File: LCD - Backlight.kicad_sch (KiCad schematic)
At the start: 1 part, among them IC2 TPS61165DBVR

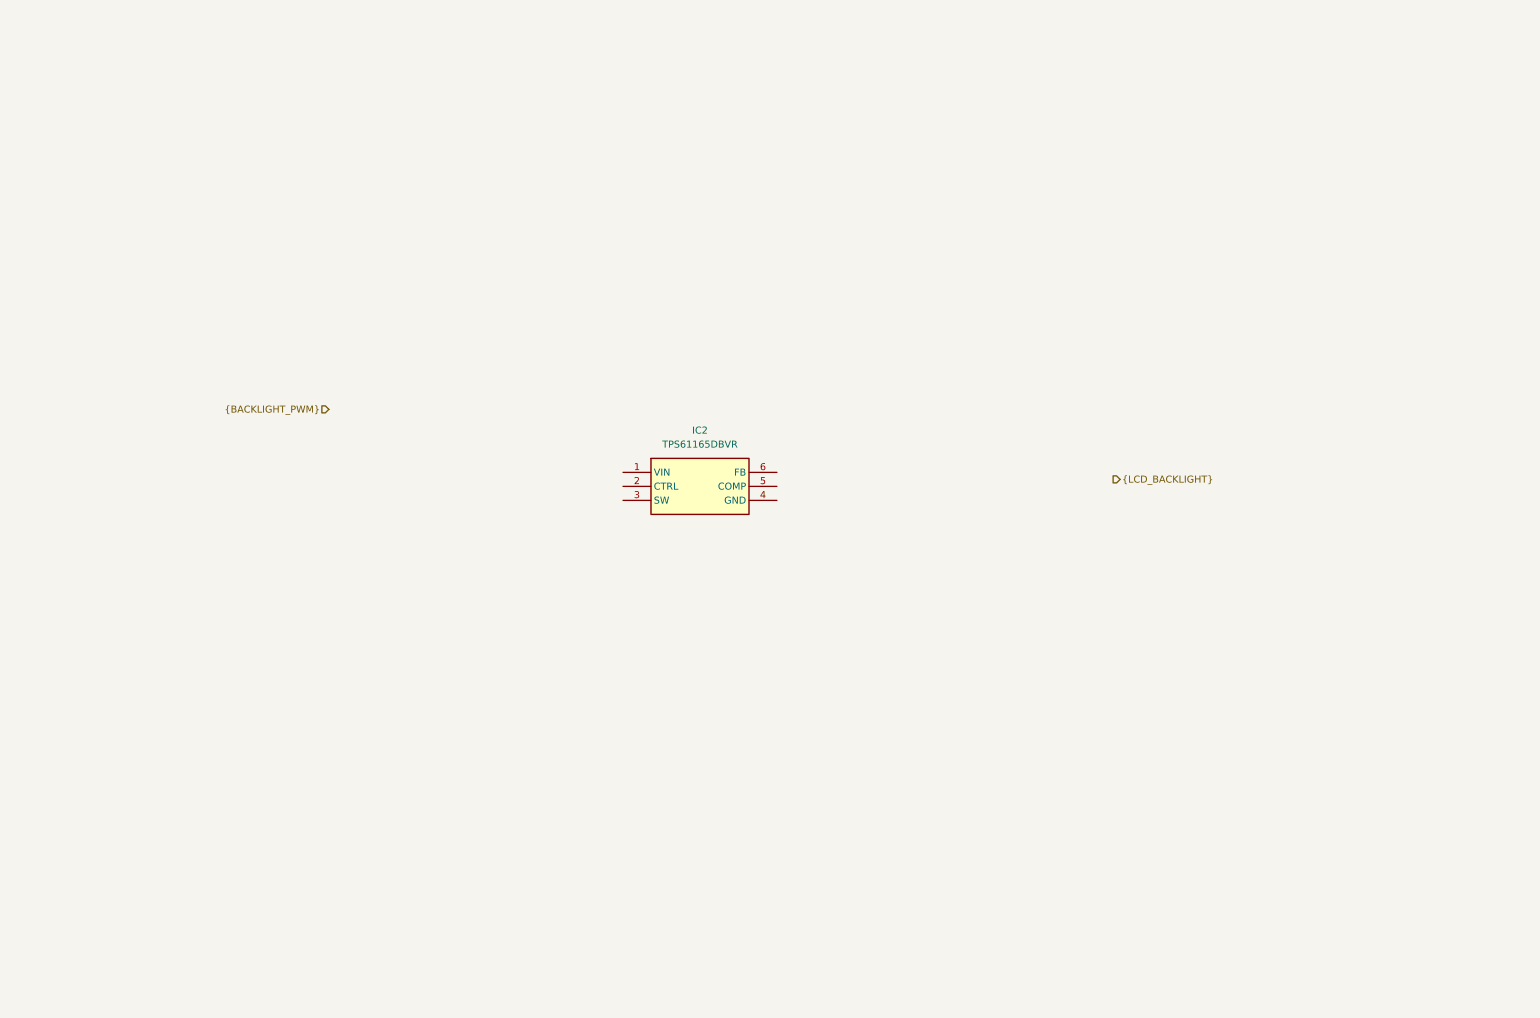
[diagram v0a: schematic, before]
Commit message: added lcd backlight schematic
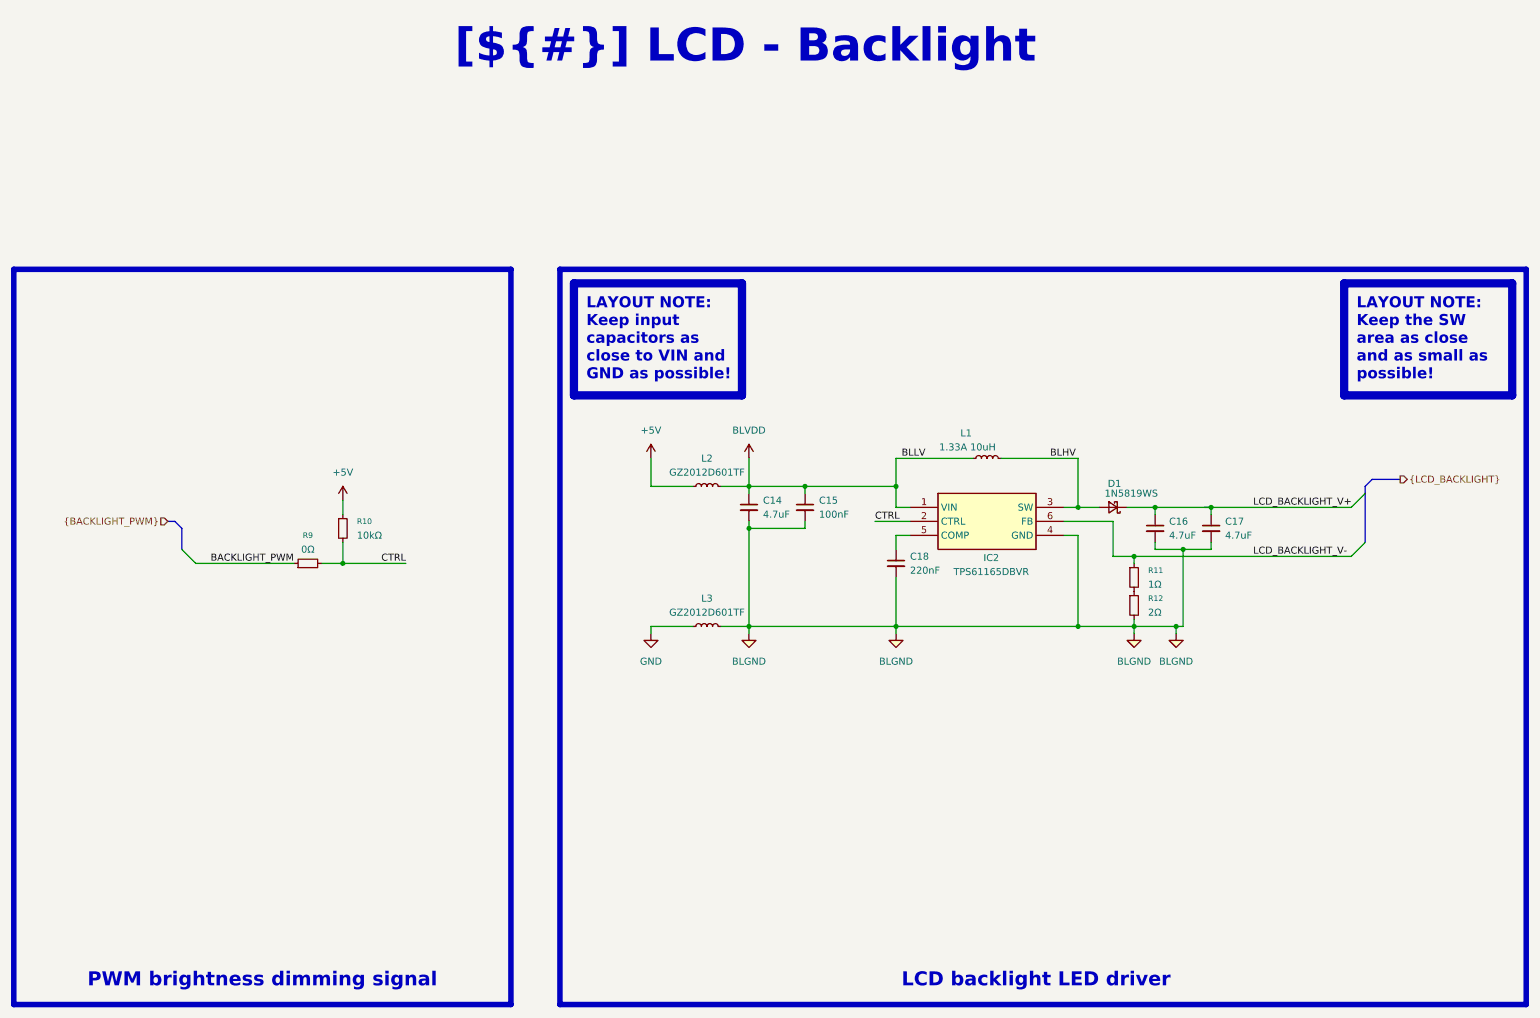
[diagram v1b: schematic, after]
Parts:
- added C14, C16, C17: 4.7uF, 0_capacitors:C_0805_2012Metric, symbol 0_capacitors:CL21A475KAQNNNE
- added C15: 100nF, 0_capacitors:C_0402_1005Metric, symbol 0_capacitors:CL05B104KO5NNNC
- added C18: 220nF, 0_capacitors:C_0402_1005Metric, symbol 0_capacitors:CL05B224KO5NNNC
- added D1: 1N5819WS, 0_diodes:D_SOD-323, symbol 0_diodes:1N5819WS
- added L1: 1.33A 10uH, 0_inductors:IND_VLS3012HBX-100M, symbol 0_inductors:VLS3012HBX-100M
- added L2, L3: GZ2012D601TF, 0_inductors:L_0805_2012Metric, symbol 0_inductors:GZ2012D601TF
- added R10: 10kΩ, 0_resistors:R_0402_1005Metric, symbol 0_resistors:0402WGF1002TCE
- added R11: 1Ω, 0_resistors:R_0603_1608Metric, symbol 0_resistors:0603WAF100KT5E
- added R12: 2Ω, 0_resistors:R_0603_1608Metric, symbol 0_resistors:0603WAF200KT5E
- added R9: 0Ω, 0_resistors:R_0402_1005Metric, symbol 0_resistors:0402WGF0000TCE
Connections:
- net BLVDD: now reaches IC2.1 (VIN)
- net BLVDD: now also C14.1, C15.1, L1.1, L2.2
- net CTRL: now reaches IC2.2 (CTRL)
- net CTRL: now also R10.2, R9.2
- net BLHV: now reaches IC2.3 (SW)
- net BLHV: now also D1.2 (A), L1.2
- net BLGND: now reaches IC2.4 (GND)
- net BLGND: now also C14.2, C15.2, C16.2, C17.2, C18.2, L3.2, R12.2
- net at IC2.5 (COMP): now also C18.1
- net LCD_BACKLIGHT_V-: now reaches IC2.6 (FB)
- net LCD_BACKLIGHT_V-: now also R11.1
- new net: R11.2, R12.1
- new net +5V: L2.1, R10.1
- new net BACKLIGHT_PWM: R9.1
- new net GND: L3.1
- new net LCD_BACKLIGHT_V+: C16.1, C17.1, D1.1 (K)
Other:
- title: (none) -> LCD - Backlight
- moved on the sheet: IC2

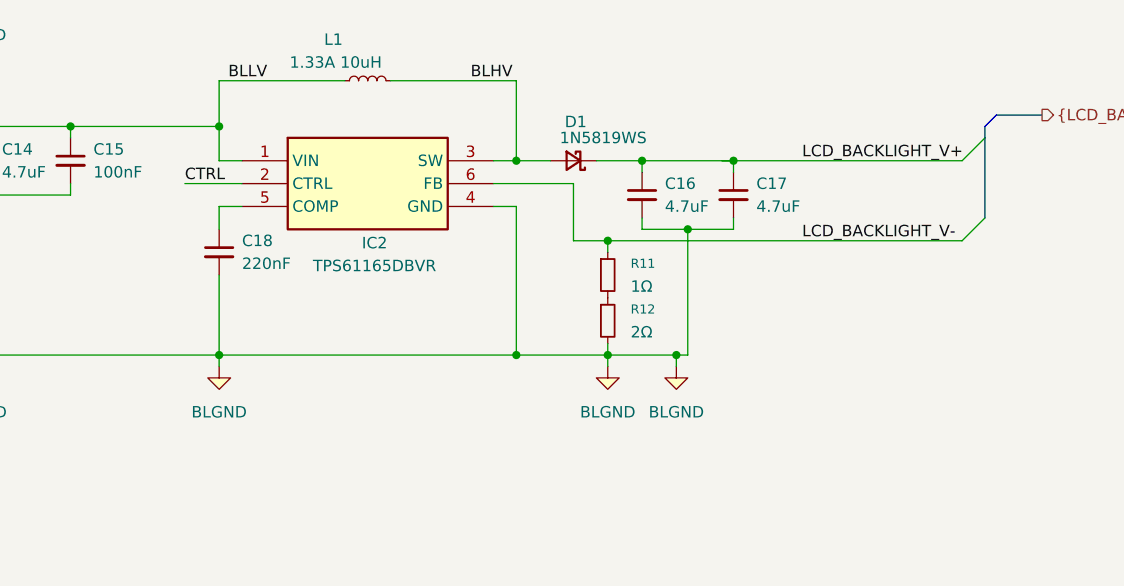
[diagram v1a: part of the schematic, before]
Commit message: added RF ransceiver
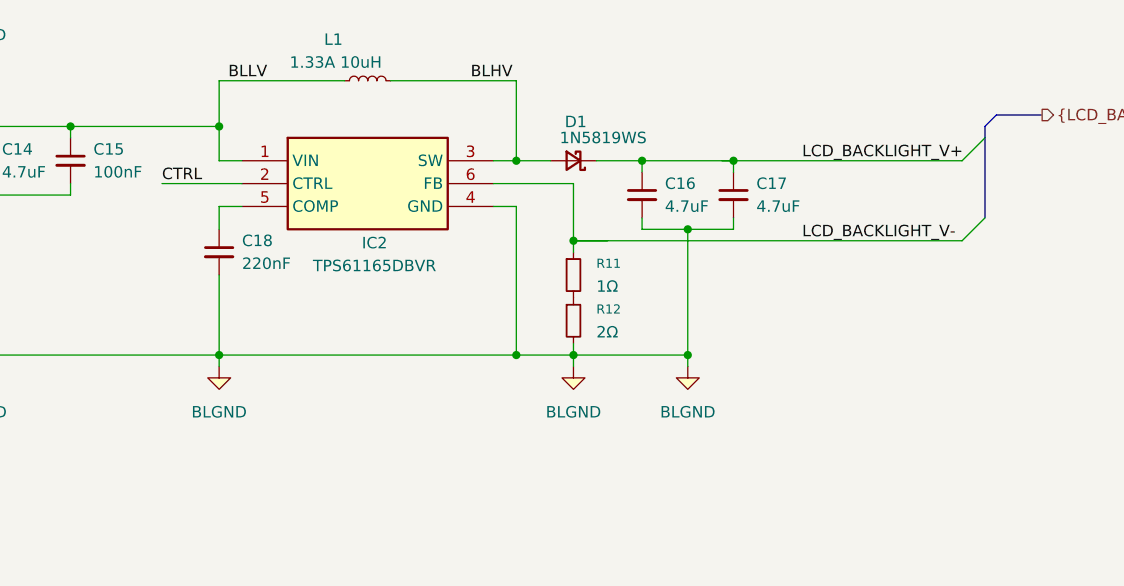
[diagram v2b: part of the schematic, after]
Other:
- moved on the sheet: R11, R12

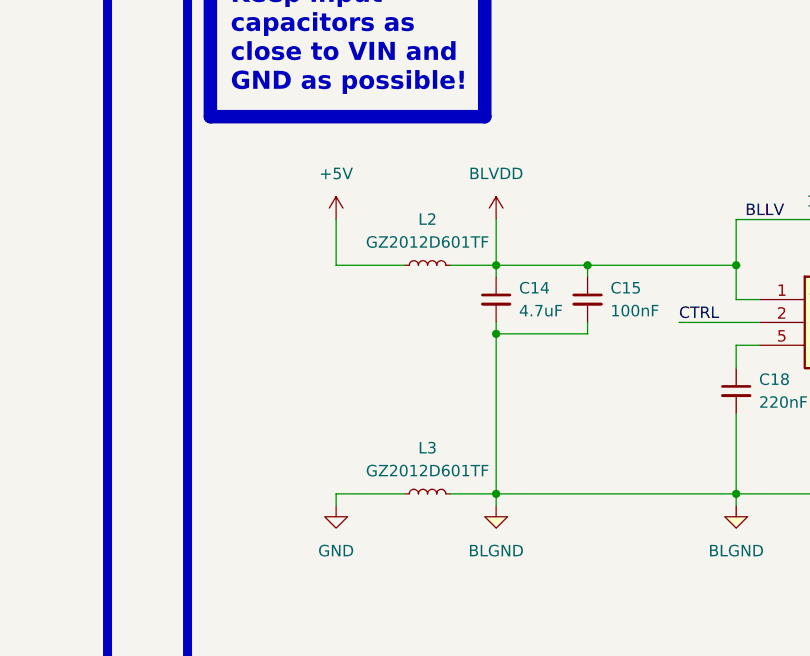
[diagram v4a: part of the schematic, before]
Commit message: added li-pol input, start creating charging circuit
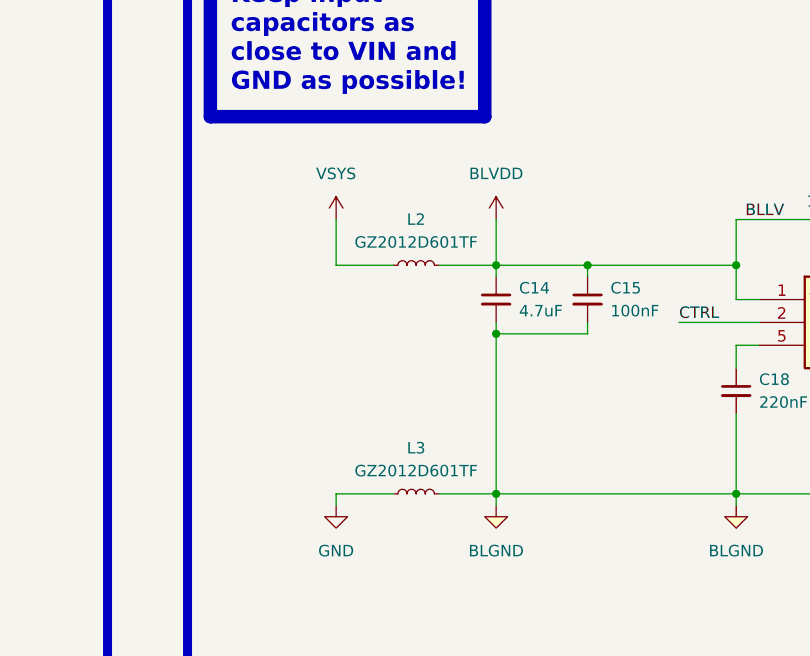
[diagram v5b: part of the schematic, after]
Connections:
- net +5V: no longer L2.1
- new net VSYS: L2.1
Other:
- moved on the sheet: L2, L3
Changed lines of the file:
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@@
 	(wire
 		(pts
-			(xy 193.04 99.06) (xy 200.66 99.06)
+			(xy 193.04 99.06) (xy 199.39 99.06)
 		)
 		(stroke
@@
 	(wire
 		(pts
-			(xy 193.04 124.46) (xy 200.66 124.46)
+			(xy 193.04 124.46) (xy 199.39 124.46)
 		)
 		(stroke
@@
 	(wire
 		(pts
-			(xy 205.74 99.06) (xy 210.82 99.06)
+			(xy 204.47 99.06) (xy 210.82 99.06)
 		)
 		(stroke
@@
 	(wire
 		(pts
-			(xy 205.74 124.46) (xy 210.82 124.46)
+			(xy 204.47 124.46) (xy 210.82 124.46)
 		)
 		(stroke
@@
 	(symbol
 		(lib_id "0_inductors:GZ2012D601TF")
-		(at 203.2 99.06 90)
+		(at 201.93 99.06 90)
 		(unit 1)
 		(exclude_from_sim no)
@@
 		(dnp no)
 		(property "Reference" "L2"
-			(at 203.2 93.98 90)
+			(at 201.93 93.98 90)
 			(effects
 				(font
@@
 		)
 		(property "Value" "GZ2012D601TF"
-			(at 203.2 96.52 90)
+			(at 201.93 96.52 90)
 			(effects
 				(font
@@
 		)
 		(property "Footprint" "0_inductors:L_0805_2012Metric"
-			(at 203.2 99.06 0)
+			(at 201.93 99.06 0)
 			(effects
 				(font
@@
 		)
 		(property "Datasheet" "~"
-			(at 203.2 99.06 0)
+			(at 201.93 99.06 0)
 			(effects
 				(font
@@
 		)
 		(property "Description" "300mΩ ±25% 600Ω@100MHz 0805 Ferrite Beads ROHS"
-			(at 203.2 99.06 0)
+			(at 201.93 99.06 0)
 			(effects
 				(font
@@
 		)
 		(property "Supplier 1" "JLCPCB"
-			(at 203.2 99.06 0)
+			(at 201.93 99.06 0)
 			(effects
 				(font
@@
 		)
 		(property "Supplier Part Number 1" "C1017"
-			(at 203.2 99.06 0)
+			(at 201.93 99.06 0)
 			(effects
 				(font
@@
 	(symbol
 		(lib_id "0_inductors:GZ2012D601TF")
-		(at 203.2 124.46 90)
+		(at 201.93 124.46 90)
 		(unit 1)
 		(exclude_from_sim no)
@@
 		(fields_autoplaced yes)
 		(property "Reference" "L3"
-			(at 203.2 119.38 90)
+			(at 201.93 119.38 90)
 			(effects
 				(font
@@
 		)
 		(property "Value" "GZ2012D601TF"
-			(at 203.2 121.92 90)
+			(at 201.93 121.92 90)
 			(effects
 				(font
@@
 		)
 		(property "Footprint" "0_inductors:L_0805_2012Metric"
-			(at 203.2 124.46 0)
+			(at 201.93 124.46 0)
 			(effects
 				(font
@@
 		)
 		(property "Datasheet" "~"
-			(at 203.2 124.46 0)
+			(at 201.93 124.46 0)
 			(effects
 				(font
@@
 		)
 		(property "Description" "300mΩ ±25% 600Ω@100MHz 0805 Ferrite Beads ROHS"
-			(at 203.2 124.46 0)
+			(at 201.93 124.46 0)
 			(effects
 				(font
@@
 		)
 		(property "Supplier 1" "JLCPCB"
-			(at 203.2 124.46 0)
+			(at 201.93 124.46 0)
 			(effects
 				(font
@@
 		)
 		(property "Supplier Part Number 1" "C1017"
-			(at 203.2 124.46 0)
+			(at 201.93 124.46 0)
 			(effects
 				(font
@@
 	)
 	(symbol
+		(lib_id "0_power_symbols:VSYS")
+		(at 193.04 93.98 0)
+		(unit 1)
+		(exclude_from_sim no)
+		(in_bom yes)
+		(on_board yes)
+		(dnp no)
+		(fields_autoplaced yes)
+		(property "Reference" "#PWR082"
+			(at 193.04 97.79 0)
+			(effects
+				(font
+					(size 1.27 1.27)
+				)
+				(hide yes)
+			)
+		)
+		(property "Value" "VSYS"
+			(at 193.04 88.9 0)
+			(effects
+				(font
+					(size 1.27 1.27)
+				)
+			)
+		)
+		(property "Footprint" ""
+			(at 193.04 93.98 0)
+			(effects
+				(font
+					(size 1.27 1.27)
+				)
+				(hide yes)
+			)
+		)
+		(property "Datasheet" ""
+			(at 193.04 93.98 0)
+			(effects
+				(font
+					(size 1.27 1.27)
+				)
+				(hide yes)
+			)
+		)
+		(property "Description" "Power symbol creates a global label with name \"VSYS\""
+			(at 193.04 93.98 0)
+			(effects
+				(font
+					(size 1.27 1.27)
+				)
+				(hide yes)
+			)
+		)
+		(pin "1"
+		)
+		(instances
+			(project ""
+				(path "/0650c7a8-acba-429c-9f8e-eec0baf0bc1c/fede4c36-00cc-4d3d-b71c-5243ba232202/d532fde6-fcc8-4703-b00a-b5308b206554"
+					(reference "#PWR082")
+					(unit 1)
+				)
+			)
+		)
+	)
+	(symbol
 		(lib_id "0_resistors:0603WAF100KT5E")
 		(at 276.86 115.57 0)
@@
 					(unit 1)
 				)
-			)
-		)
-	)
-	(symbol
-		(lib_id "power:+5V")
-		(at 193.04 93.98 0)
-		(unit 1)
-		(exclude_from_sim no)
-		(in_bom yes)
-		(on_board yes)
-		(dnp no)
-		(fields_autoplaced yes)
-		(property "Reference" "#PWR026"
-			(at 193.04 97.79 0)
-			(effects
-				(font
-					(size 1.27 1.27)
-				)
-				(hide yes)
-			)
-		)
-		(property "Value" "+5V"
-			(at 193.04 88.9 0)
-			(effects
-				(font
-					(size 1.27 1.27)
-				)
-			)
-		)
-		(property "Footprint" ""
-			(at 193.04 93.98 0)
-			(effects
-				(font
-					(size 1.27 1.27)
-				)
-				(hide yes)
-			)
-		)
-		(property "Datasheet" ""
-			(at 193.04 93.98 0)
-			(effects
-				(font
-					(size 1.27 1.27)
-				)
-				(hide yes)
-			)
-		)
-		(property "Description" "Power symbol creates a global label with name \"+5V\""
-			(at 193.04 93.98 0)
-			(effects
-				(font
-					(size 1.27 1.27)
-				)
-				(hide yes)
-			)
-		)
-		(pin "1"
-		)
-		(instances
-			(project "transmitter"
-				(path "/0650c7a8-acba-429c-9f8e-eec0baf0bc1c/fede4c36-00cc-4d3d-b71c-5243ba232202/d532fde6-fcc8-4703-b00a-b5308b206554"
-					(reference "#PWR026")
-					(unit 1)
-				)
